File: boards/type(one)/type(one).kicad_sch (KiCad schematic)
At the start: 41 parts, among them J1 IDC-Header_02x03, J2 IDC-Header_02x05, J3 Conn_01x02, J4 Conn_01x05, J5 Conn_01x05, J6 Conn_01x03, J7 Conn_01x02, J8 Conn_01x02, Q1 2N2907, Q2 2n2222, Q3 IRF4905, Q4 2N7000, U1 ESP32-WROOM-UE, U2 LM393, U3 LM7805_TO220, U5 LM1117DT-ADJ

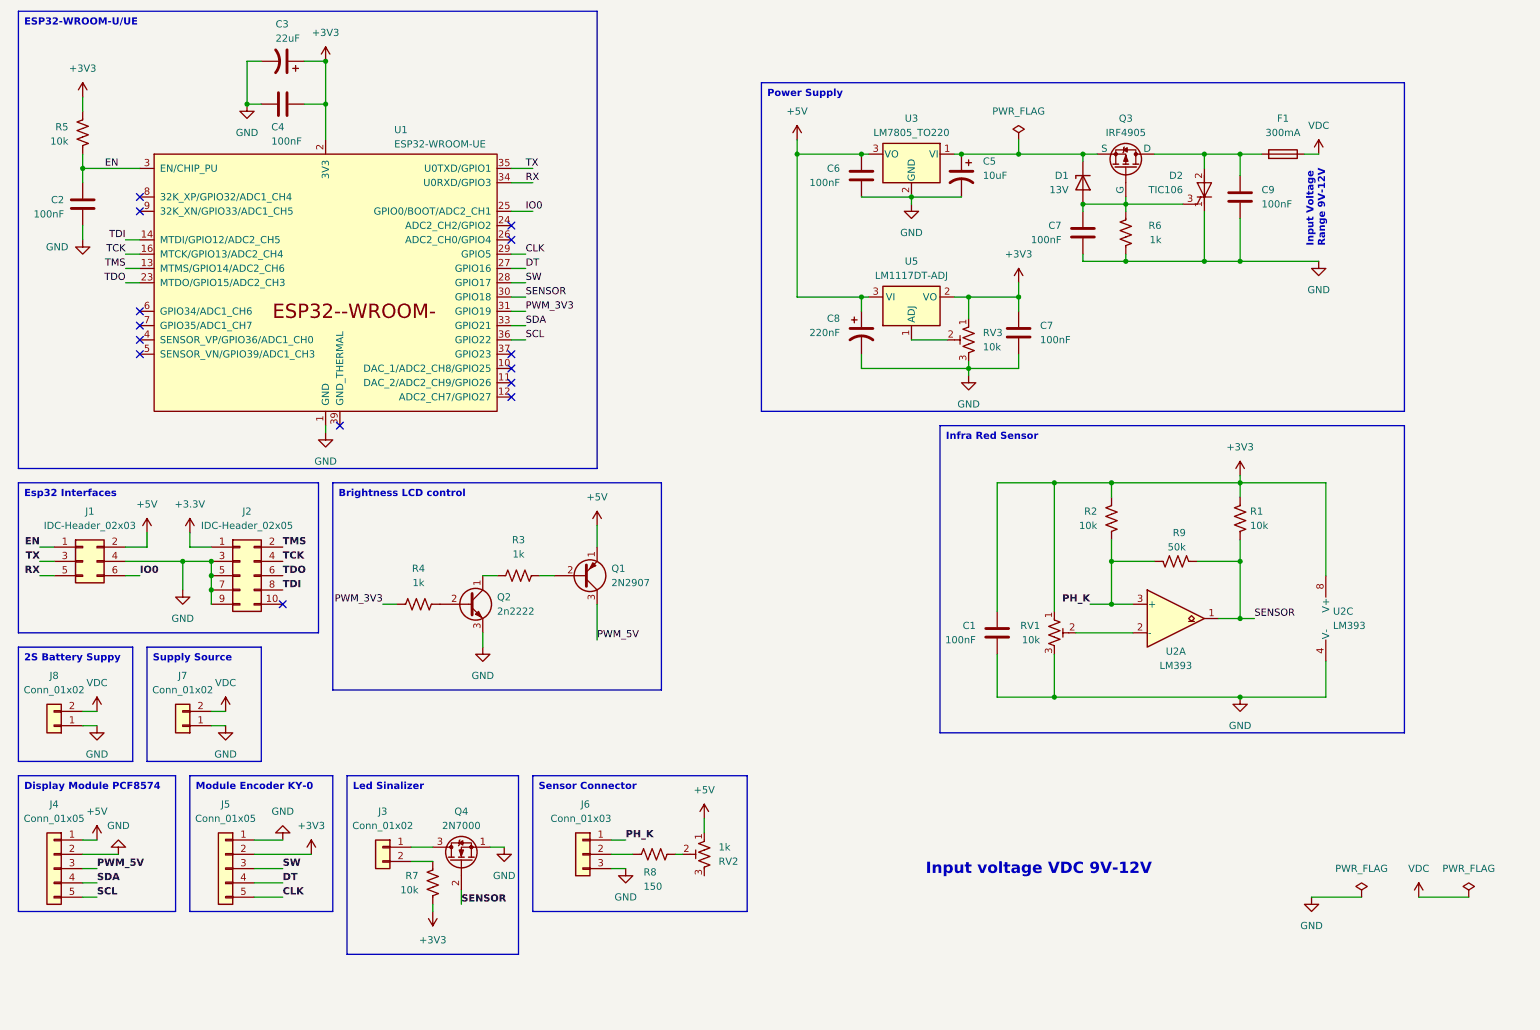
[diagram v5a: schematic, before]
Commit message: add battery support
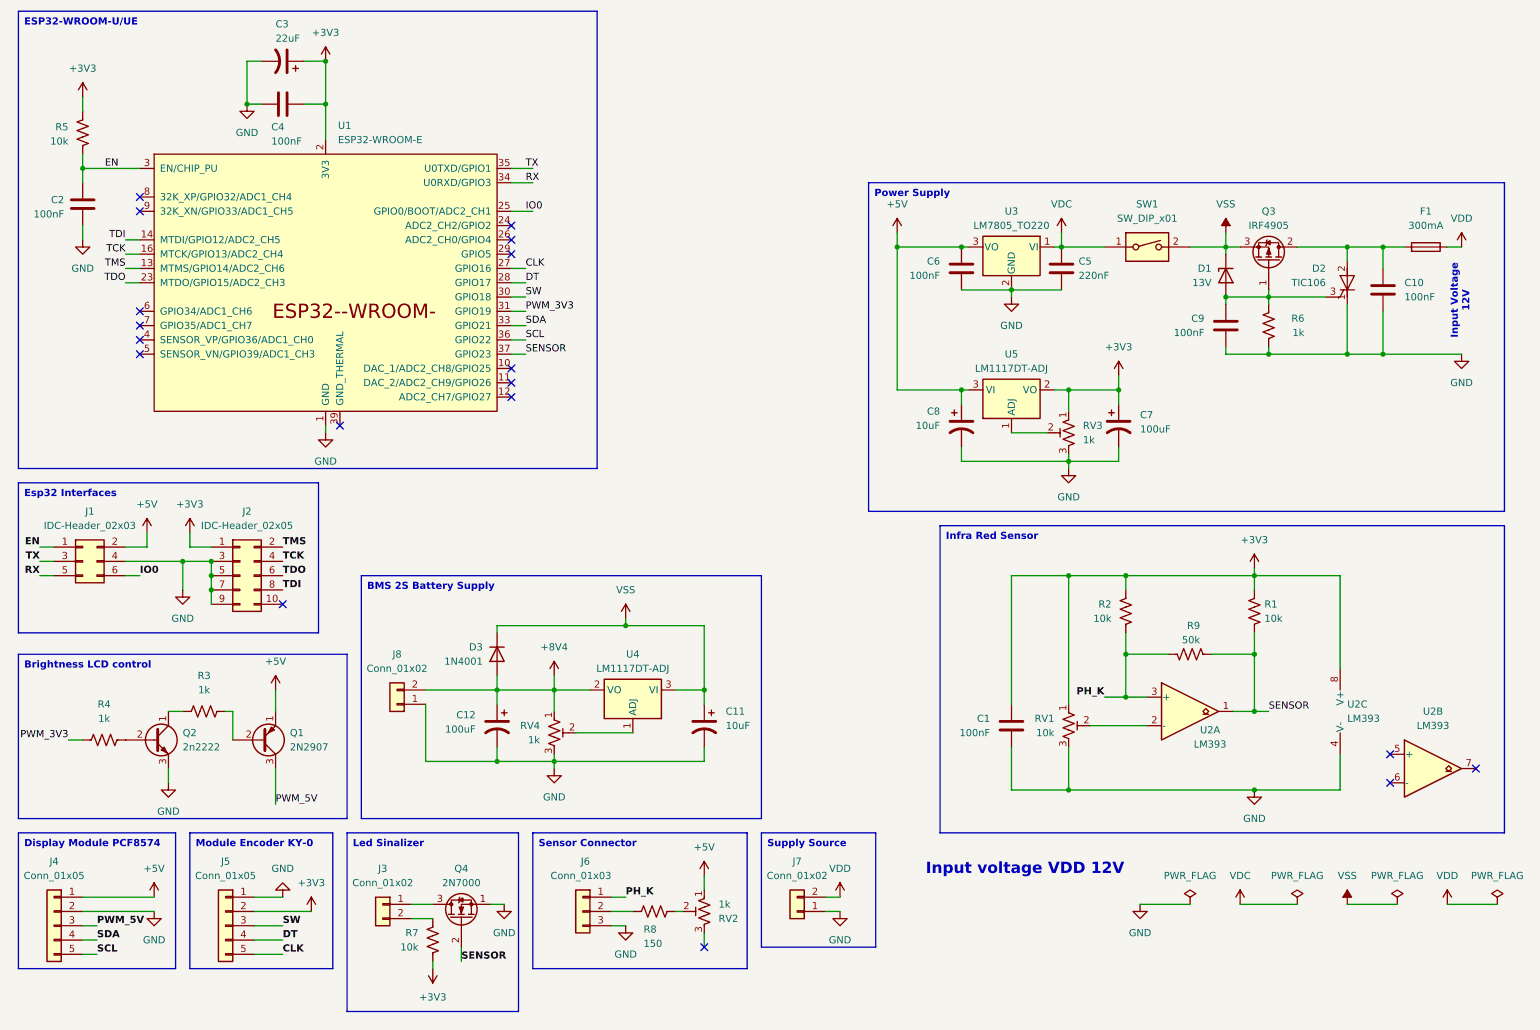
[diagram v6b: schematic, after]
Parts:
- removed Q3: IRF4905, Package_TO_SOT_THT:TO-220-3_Vertical, symbol Simulation_SPICE:PMOS
- added C11: 10uF, Capacitor_THT:CP_Radial_Tantal_D5.5mm_P2.50mm, symbol Device:C_Polarized_US
- added C12: 100uF, symbol Device:C_Polarized_US
- added D3: 1N4001, Diode_THT:D_DO-41_SOD81_P10.16mm_Horizontal, symbol Diode:1N4001
- added Q3: IRF4905, Package_TO_SOT_THT:TO-220-3_Vertical, symbol Transistor_FET:IRF4905
- added RV4: 1k, Potentiometer_THT:Potentiometer_Bourns_3386X_Horizontal, symbol Device:R_Potentiometer_Trim_US
- added SW1: SW_DIP_x01, symbol Switch:SW_DIP_x01
- added unit 2 of U2
- added U4: LM1117DT-ADJ, Package_TO_SOT_SMD:TO-252-3_TabPin2, symbol Regulator_Linear:LM1117DT-ADJ
- C5: value 10uF -> 220nF; symbol Device:C_Polarized_US -> Device:C
- C7: value 100nF -> 100uF; symbol Device:C -> Device:C_Polarized_US
- C8: value 220nF -> 10uF
- RV3: value 10k -> 1k
- U1: value ESP32-WROOM-UE -> ESP32-WROOM-E; footprint PCM_Espressif:ESP32-WROOM-32UE -> PCM_Espressif:ESP32-WROOM-32E
- U2: footprint Package_DIP:DIP-8_W7.62mm -> (none)
- renumbered C9 to C10, C7 to C9
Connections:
- net +3.3V is gone; now on net +3V3: J2.1 (Pin_1)
- net CLK: now also U1.27 (GPIO16); no longer U1.29 (GPIO5)
- net DT: now also U1.28 (GPIO17); no longer U1.27 (GPIO16)
- net GND: now also C11.2, C12.2, RV4.3
- net SENSOR: now also U1.37 (GPIO23); no longer U1.30 (GPIO18)
- net SW: now also U1.30 (GPIO18); no longer U1.28 (GPIO17)
- net VDC: now also C5.1, U3.1 (VI), SW1.1; no longer F1.1, J7.2 (Pin_2), J8.2 (Pin_2)
- net at C10.1, D2.2 (A), F1.2: now also Q3.2 (D)
- net at C9.1, D1.2 (A), D2.3 (G)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: now also Q3.1 (G)
- new net: RV4.2, U4.1 (ADJ)
- new net +8V4: C12.1, D3.2 (A), J8.2 (Pin_2), RV4.1, U4.2 (VO)
- new net VDD: F1.1, J7.2 (Pin_2)
- new net VSS: C11.1, D1.1 (K), D3.1 (K), Q3.3 (S), SW1.2, U4.3 (VI)
- no-connect marks 14 -> 18
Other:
- note added: "Input Voltage 12V"
- note added: "Input voltage VDD 12V"
- note removed: "Input Voltage Range 9V-12V"
- note removed: "Input voltage VDC 9V-12V"
- moved on the sheet: C1, C10, C6, C8, C9, D1, D2, F1, J3, J4, J5, J6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

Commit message: create pcb and update circuit
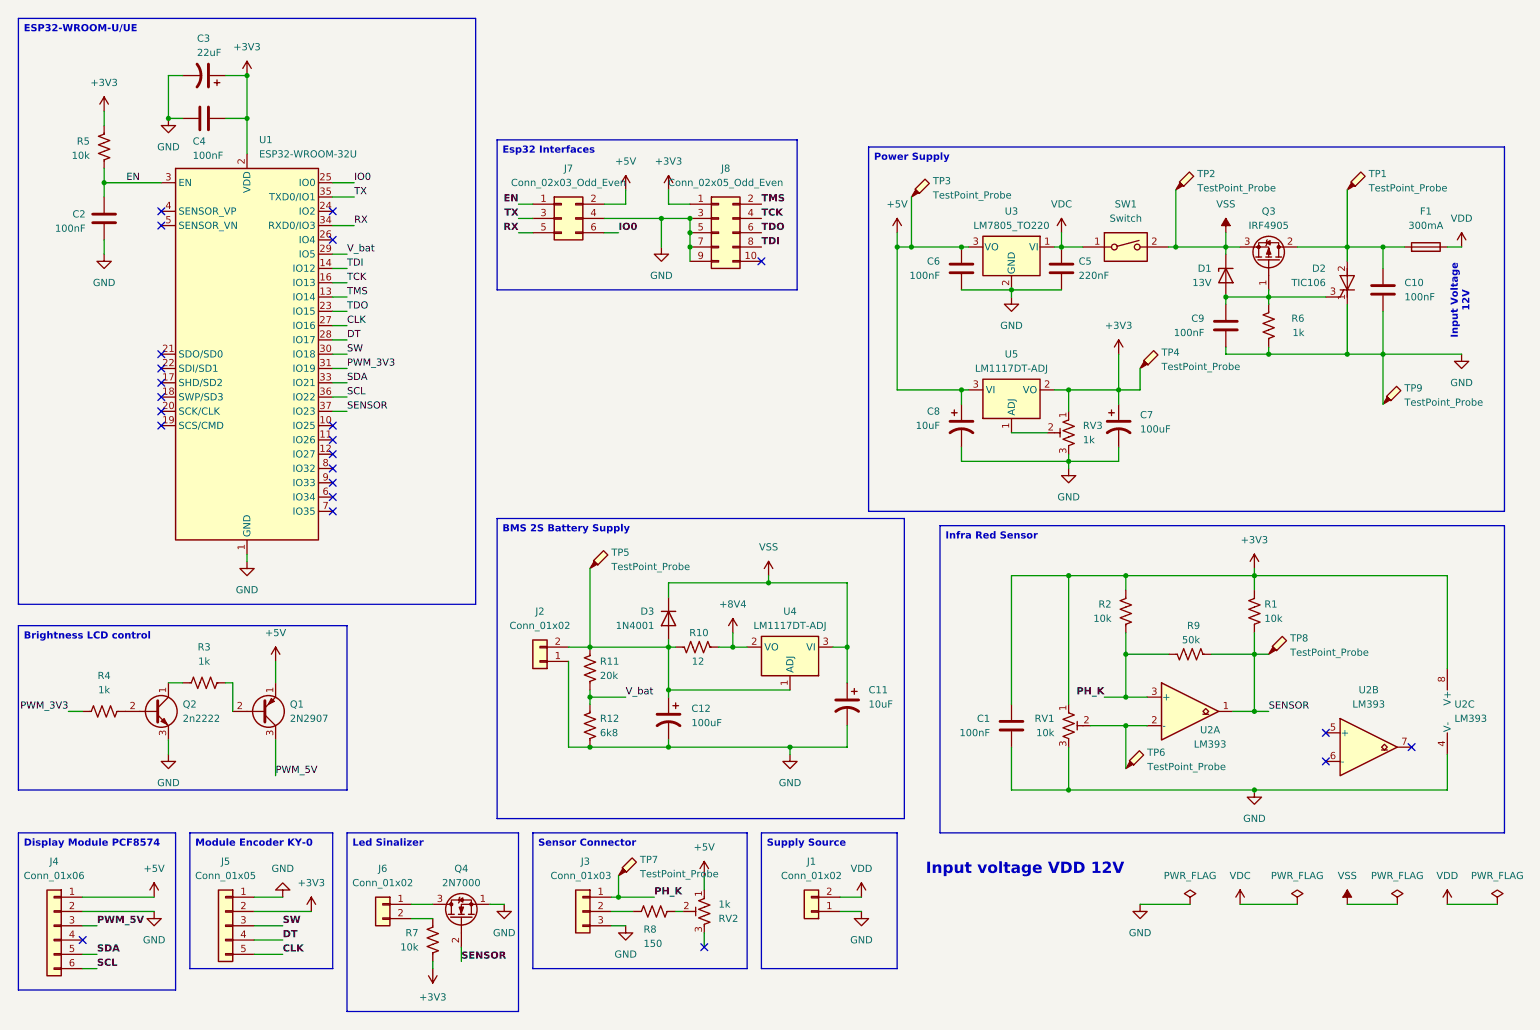
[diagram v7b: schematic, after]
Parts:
- removed RV4: 1k, Potentiometer_THT:Potentiometer_Bourns_3386X_Horizontal, symbol Device:R_Potentiometer_Trim_US
- removed U1: ESP32-WROOM-E, PCM_Espressif:ESP32-WROOM-32E, symbol PCM_Espressif:ESP32-WROOM-E
- added R10: 12, Resistor_THT:R_Axial_DIN0207_L6.3mm_D2.5mm_P7.62mm_Horizontal, symbol Device:R_US
- added R11: 20k, Resistor_THT:R_Axial_DIN0207_L6.3mm_D2.5mm_P7.62mm_Horizontal, symbol Device:R_US
- added R12: 6k8, Resistor_THT:R_Axial_DIN0207_L6.3mm_D2.5mm_P7.62mm_Horizontal, symbol Device:R_US
- added TP1, TP2, TP3, TP4, TP5, TP6, TP7, TP8, TP9: TestPoint_Probe, TestPoint:TestPoint_THTPad_3.0x3.0mm_Drill1.5mm, symbol Connector:TestPoint_Probe
- added U1: ESP32-WROOM-32U, RF_Module:ESP32-WROOM-32, symbol RF_Module:ESP32-WROOM-32U
- C12: footprint (none) -> Capacitor_THT:CP_Radial_D5.0mm_P2.50mm
- C5: footprint Capacitor_THT:CP_Radial_Tantal_D5.5mm_P2.50mm -> Capacitor_THT:C_Rect_L7.0mm_W2.5mm_P5.00mm
- C6: footprint (none) -> Capacitor_THT:C_Disc_D5.0mm_W2.5mm_P5.00mm
- C7: footprint (none) -> Capacitor_THT:CP_Radial_Tantal_D5.5mm_P2.50mm
- J4: value Conn_01x05 -> Conn_01x06; footprint Connector_Molex:Molex_KK-254_AE-6410-05A_1x05_P2.54mm_Vertical -> Connector_Molex:Molex_KK-254_AE-6410-06A_1x06_P2.54mm_Vertical; symbol Connector_Generic:Conn_01x05 -> Connector_Generic:Conn_01x06
- J7: renamed from J1; value IDC-Header_02x03 -> Conn_02x03_Odd_Even
- J8: renamed from J2; value IDC-Header_02x05 -> Conn_02x05_Odd_Even
- SW1: value SW_DIP_x01 -> Switch; footprint (none) -> Connector_Molex:Molex_KK-254_AE-6410-02A_1x02_P2.54mm_Vertical
- U2: footprint (none) -> Package_DIP:DIP-8_W7.62mm
- U4, U5: footprint Package_TO_SOT_SMD:TO-252-3_TabPin2 -> Package_TO_SOT_THT:TO-220-3_Vertical
- renumbered J7 to J1, J8 to J2, J6 to J3, J3 to J6
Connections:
- net +3V3: now also TP4.1, U1.2 (VDD)
- net +5V: now also TP3.1
- net +8V4: now also R10.2; no longer C12.1, D3.2 (A), J2.2 (Pin_2)
- net CLK: now also U1.27 (IO16)
- net DT: now also U1.28 (IO17)
- net EN: now also U1.3 (EN)
- net GND: now also R12.2, TP9.1, U1.1 (GND), U1.15 (GND), U1.38 (GND), U1.39 (GND)
- net IO0: now also U1.25 (IO0)
- net PH_K: now also TP7.1
- net PWM_3V3: now also U1.31 (IO19)
- net RX: now also U1.34 (RXD0/IO3)
- net SCL: now also J4.6 (Pin_6), U1.36 (IO22); no longer J4.5 (Pin_5)
- net SDA: now also J4.5 (Pin_5), U1.33 (IO21); no longer J4.4 (Pin_4)
- net SENSOR: now also TP8.1, U1.37 (IO23)
- net SW: now also U1.30 (IO18)
- net TCK: now also U1.16 (IO13)
- net TDI: now also U1.14 (IO12)
- net TDO: now also U1.23 (IO15)
- net TMS: now also U1.13 (IO14)
- net TX: now also U1.35 (TXD0/IO1)
- net VSS: now also TP2.1
- net at U4.1 (ADJ): now also C12.1, D3.2 (A), J2.2 (Pin_2), R10.1, R11.1, TP5.1
- net at RV1.2, U2.2 (-): now also TP6.1
- net at C10.1, D2.2 (A), F1.2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: now also TP1.1
- new net V_bat: R11.2, R12.1, U1.29 (IO5)
- no-connect marks 18 -> 23
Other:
- moved on the sheet: C11, C12, C2, C3, C4, D3, J1, J2, J7, J8, Q2, R3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
